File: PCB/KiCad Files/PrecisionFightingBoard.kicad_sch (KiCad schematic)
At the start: 6 parts, among them J1 Screw_Terminal_01x05, J2 Screw_Terminal_01x05, J3 Screw_Terminal_01x05, J4 Screw_Terminal_01x05, J5 Conn_02x10_Odd_Even, U1 Teensy4.0

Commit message: add mounting hole
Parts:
- added H1, H2, H3, H4: MountingHole, symbol Mechanical:MountingHole
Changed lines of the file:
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@@
     (pin "5")
     (instances
-      (project "Teensy"
+      (project "PrecisionFightingBoard"
         (path "/01d790aa-01e7-46c4-a23c-7deb91137dd0"
           (reference "J2") (unit 1)
+        )
+      )
+    )
+  )
+  (symbol (lib_id "Mechanical:MountingHole") (at 24.13 99.06 0) (unit 1)
+    (in_bom yes) (on_board yes) (dnp no) (fields_autoplaced)
+    (property "Reference" "H2" (at 26.67 97.79 0)
+      (effects (font (size 1.27 1.27)) (justify left))
+    )
+    (property "Value" "MountingHole" (at 26.67 100.33 0)
+      (effects (font (size 1.27 1.27)) (justify left))
+    )
+    (property "Footprint" "" (at 24.13 99.06 0)
+      (effects (font (size 1.27 1.27)) hide)
+    )
+    (property "Datasheet" "~" (at 24.13 99.06 0)
+      (effects (font (size 1.27 1.27)) hide)
+    )
+    (instances
+      (project "PrecisionFightingBoard"
+        (path "/01d790aa-01e7-46c4-a23c-7deb91137dd0"
+          (reference "H2") (unit 1)
+        )
+      )
+    )
+  )
+  (symbol (lib_id "Mechanical:MountingHole") (at 24.13 106.68 0) (unit 1)
+    (in_bom yes) (on_board yes) (dnp no) (fields_autoplaced)
+    (property "Reference" "H3" (at 26.67 105.41 0)
+      (effects (font (size 1.27 1.27)) (justify left))
+    )
+    (property "Value" "MountingHole" (at 26.67 107.95 0)
+      (effects (font (size 1.27 1.27)) (justify left))
+    )
+    (property "Footprint" "" (at 24.13 106.68 0)
+      (effects (font (size 1.27 1.27)) hide)
+    )
+    (property "Datasheet" "~" (at 24.13 106.68 0)
+      (effects (font (size 1.27 1.27)) hide)
+    )
+    (instances
+      (project "PrecisionFightingBoard"
+        (path "/01d790aa-01e7-46c4-a23c-7deb91137dd0"
+          (reference "H3") (unit 1)
         )
       )
@@
     (pin "4")
     (instances
-      (project "Teensy"
+      (project "PrecisionFightingBoard"
         (path "/01d790aa-01e7-46c4-a23c-7deb91137dd0"
           (reference "U1") (unit 1)
@@
     )
   )
+  (symbol (lib_id "Mechanical:MountingHole") (at 24.13 91.44 0) (unit 1)
+    (in_bom yes) (on_board yes) (dnp no) (fields_autoplaced)
+    (property "Reference" "H1" (at 26.67 90.17 0)
+      (effects (font (size 1.27 1.27)) (justify left))
+    )
+    (property "Value" "MountingHole" (at 26.67 92.71 0)
+      (effects (font (size 1.27 1.27)) (justify left))
+    )
+    (property "Footprint" "" (at 24.13 91.44 0)
+      (effects (font (size 1.27 1.27)) hide)
+    )
+    (property "Datasheet" "~" (at 24.13 91.44 0)
+      (effects (font (size 1.27 1.27)) hide)
+    )
+    (instances
+      (project "PrecisionFightingBoard"
+        (path "/01d790aa-01e7-46c4-a23c-7deb91137dd0"
+          (reference "H1") (unit 1)
+        )
+      )
+    )
+  )
+  (symbol (lib_id "Mechanical:MountingHole") (at 24.13 114.3 0) (unit 1)
+    (in_bom yes) (on_board yes) (dnp no) (fields_autoplaced)
+    (property "Reference" "H4" (at 26.67 113.03 0)
+      (effects (font (size 1.27 1.27)) (justify left))
+    )
+    (property "Value" "MountingHole" (at 26.67 115.57 0)
+      (effects (font (size 1.27 1.27)) (justify left))
+    )
+    (property "Footprint" "" (at 24.13 114.3 0)
+      (effects (font (size 1.27 1.27)) hide)
+    )
+    (property "Datasheet" "~" (at 24.13 114.3 0)
+      (effects (font (size 1.27 1.27)) hide)
+    )
+    (instances
+      (project "PrecisionFightingBoard"
+        (path "/01d790aa-01e7-46c4-a23c-7deb91137dd0"
+          (reference "H4") (unit 1)
+        )
+      )
+    )
+  )
   (symbol (lib_id "Connector:Screw_Terminal_01x05") (at 45.72 74.93 0) (unit 1)
     (in_bom yes) (on_board yes) (dnp no) (fields_autoplaced)
@@
     (pin "5")
     (instances
-      (project "Teensy"
+      (project "PrecisionFightingBoard"
         (path "/01d790aa-01e7-46c4-a23c-7deb91137dd0"
           (reference "J4") (unit 1)
@@
     (pin "5")
     (instances
-      (project "Teensy"
+      (project "PrecisionFightingBoard"
         (path "/01d790aa-01e7-46c4-a23c-7deb91137dd0"
           (reference "J3") (unit 1)
@@
     (pin "5")
     (instances
-      (project "Teensy"
+      (project "PrecisionFightingBoard"
         (path "/01d790aa-01e7-46c4-a23c-7deb91137dd0"
           (reference "J1") (unit 1)
@@
     (pin "9")
     (instances
-      (project "Teensy"
+      (project "PrecisionFightingBoard"
         (path "/01d790aa-01e7-46c4-a23c-7deb91137dd0"
           (reference "J5") (unit 1)

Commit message: Create a schematic
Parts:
- removed J1, J2, J3, J4: Screw_Terminal_01x05, symbol Connector:Screw_Terminal_01x05
- removed J5: Conn_02x10_Odd_Even, symbol Connector_Generic:Conn_02x10_Odd_Even
- added J10, J7, J8, J9: ST01x05, TerminalBlock_MetzConnect:TerminalBlock_MetzConnect_Type059_RT06305HBWC_1x05_P3.50mm_Horizontal, symbol Connector:Screw_Terminal_01x05
- added J6: Conn_02x10_Odd_Even, Connector_PinHeader_2.54mm:PinHeader_2x10_P2.54mm_Vertical, symbol Connector_Generic:Conn_02x10_Odd_Even
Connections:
- net GND: now reaches U1.1 (GND)
- net GND: now also J10.5 (Pin_5), J6.12 (Pin_12), J6.17 (Pin_17), J6.18 (Pin_18), J8.1 (Pin_1), J8.2 (Pin_2), J9.5 (Pin_5)
- net X: now reaches U1.10 (8_TX2_IN1)
- net X: now also J6.8 (Pin_8), J9.1 (Pin_1)
- net RB: now reaches U1.11 (9_OUT1C)
- net RB: now also J6.10 (Pin_10), J9.3 (Pin_3)
- net LB: now reaches U1.12 (10_CS_MQSR)
- net LB: now also J6.11 (Pin_11), J9.4 (Pin_4)
- net A: now reaches U1.13 (11_MOSI_CTX1)
- net A: now also J10.1 (Pin_1), J6.13 (Pin_13)
- net B: now reaches U1.14 (12_MISO_MQSL)
- net B: now also J10.2 (Pin_2), J6.14 (Pin_14)
- net UP: now reaches U1.2 (0_RX1_CRX2_CS1)
- net UP: now also J6.1 (Pin_1), J7.3 (Pin_3)
- net RT: now reaches U1.21 (14_A0_TX3_SPDIF_OUT)
- net RT: now also J10.3 (Pin_3), J6.15 (Pin_15)
- net LT: now reaches U1.22 (15_A1_RX3_SPDIF_IN)
- net LT: now also J10.4 (Pin_4), J6.16 (Pin_16)
- net L3: now reaches U1.25 (18_A4_SDA0)
- net R3: now reaches U1.26 (19_A5_SCL0)
- net DOWN: now reaches U1.3 (1_TX1_CTX2_MISO1)
- net DOWN: now also J6.2 (Pin_2), J7.2 (Pin_2)
- net LEFT: now reaches U1.4 (2_OUT2)
- net LEFT: now also J6.4 (Pin_4), J7.4 (Pin_4)
- net RIGHT: now reaches U1.5 (3_LRCLK2)
- net RIGHT: now also J6.3 (Pin_3), J7.5 (Pin_5)
- net HOME: now reaches U1.6 (4_BCLK2)
- net HOME: now also J6.6 (Pin_6), J8.3 (Pin_3)
- net BACK: now reaches U1.7 (5_IN2)
- net BACK: now also J6.5 (Pin_5), J8.4 (Pin_4)
- net START: now reaches U1.8 (6_OUT1D)
- net START: now also J6.7 (Pin_7), J8.5 (Pin_5)
- net Y: now reaches U1.9 (7_RX2_OUT1A)
- net Y: now also J6.9 (Pin_9), J9.2 (Pin_2)
- new net 5V: J6.19 (Pin_19), J6.20 (Pin_20), J7.1 (Pin_1)
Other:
- moved on the sheet: H1, H2, H3, H4, U1

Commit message: add GND wire
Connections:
- net GND: now also U1.32 (GND)
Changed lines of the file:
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@@
+    (stroke (width 0) (type default))
+  )
+  (wire (pts (xy 175.26 83.82) (xy 176.53 83.82))
     (stroke (width 0) (type default))
   )
@@
     (effects (font (size 1.27 1.27)) (justify left bottom))
   )
+  (label "GND" (at 176.53 83.82 0) (fields_autoplaced)
+    (effects (font (size 1.27 1.27)) (justify left bottom))
+  )

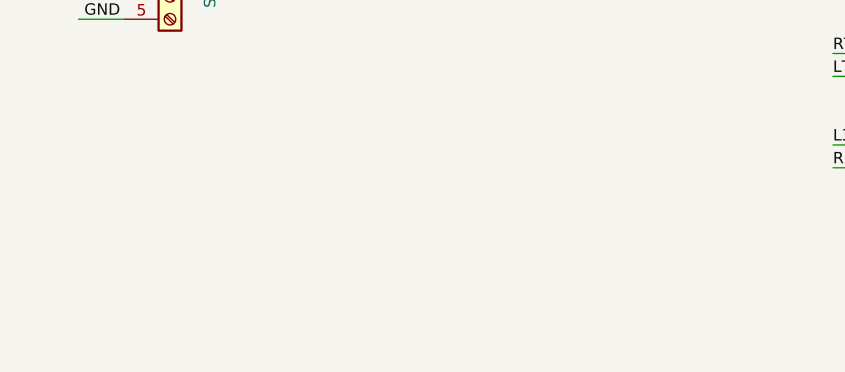
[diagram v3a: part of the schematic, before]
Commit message: add connector
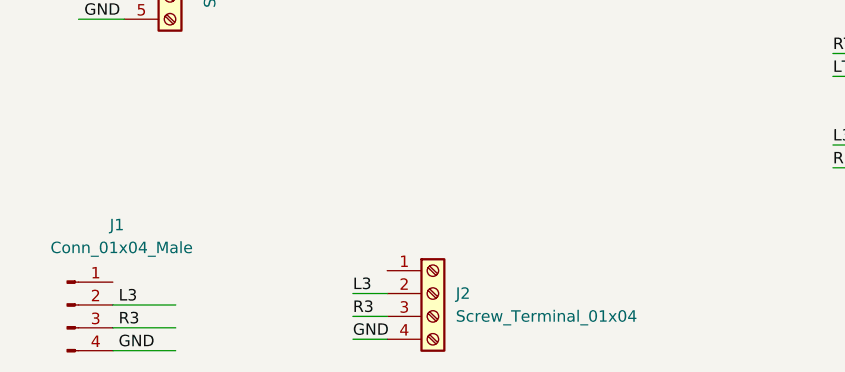
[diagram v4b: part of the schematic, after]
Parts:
- added J1: Conn_01x04_Male, Connector_JST:JST_PH_B4B-PH-K_1x04_P2.00mm_Vertical, symbol Connector:Conn_01x04_Male
- added J2: Screw_Terminal_01x04, symbol Connector:Screw_Terminal_01x04
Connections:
- net GND: now also J1.4 (Pin_4), J2.4 (Pin_4)
- net L3: now also J1.2 (Pin_2), J2.2 (Pin_2)
- net R3: now also J1.3 (Pin_3), J2.3 (Pin_3)
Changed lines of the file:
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@@
+    (stroke (width 0) (type default))
+  )
+  (wire (pts (xy 60.96 102.87) (xy 64.77 102.87))
     (stroke (width 0) (type default))
   )
@@
     (stroke (width 0) (type default))
   )
+  (wire (pts (xy 41.275 101.6) (xy 34.29 101.6))
+    (stroke (width 0) (type default))
+  )
   (wire (pts (xy 92.71 58.42) (xy 85.09 58.42))
     (stroke (width 0) (type default))
@@
     (stroke (width 0) (type default))
   )
+  (wire (pts (xy 41.275 104.14) (xy 34.29 104.14))
+    (stroke (width 0) (type default))
+  )
   (wire (pts (xy 35.56 46.99) (xy 30.48 46.99))
     (stroke (width 0) (type default))
@@
     (stroke (width 0) (type default))
   )
+  (wire (pts (xy 41.275 106.68) (xy 34.29 106.68))
+    (stroke (width 0) (type default))
+  )
   (wire (pts (xy 35.56 62.23) (xy 30.48 62.23))
     (stroke (width 0) (type default))
   )
+  (wire (pts (xy 60.96 100.33) (xy 64.77 100.33))
+    (stroke (width 0) (type default))
+  )
   (wire (pts (xy 35.56 69.85) (xy 30.48 69.85))
     (stroke (width 0) (type default))
@@
     (stroke (width 0) (type default))
   )
+  (wire (pts (xy 60.96 105.41) (xy 64.77 105.41))
+    (stroke (width 0) (type default))
+  )
   (label "START" (at 31.115 44.45 0) (fields_autoplaced)
     (effects (font (size 1.27 1.27)) (justify left bottom))
@@
     (effects (font (size 1.27 1.27)) (justify left bottom))
   )
+  (label "R3" (at 60.96 102.87 0) (fields_autoplaced)
+    (effects (font (size 1.27 1.27)) (justify left bottom))
+  )
   (label "BACK" (at 114.3 38.1 0) (fields_autoplaced)
     (effects (font (size 1.27 1.27)) (justify left bottom))
@@
     (effects (font (size 1.27 1.27)) (justify left bottom))
   )
+  (label "L3" (at 60.96 100.33 0) (fields_autoplaced)
+    (effects (font (size 1.27 1.27)) (justify left bottom))
+  )
   (label "GND" (at 31.115 69.85 0) (fields_autoplaced)
     (effects (font (size 1.27 1.27)) (justify left bottom))
@@
     (effects (font (size 1.27 1.27)) (justify left bottom))
   )
+  (label "L3" (at 34.925 101.6 0) (fields_autoplaced)
+    (effects (font (size 1.27 1.27)) (justify left bottom))
+  )
+  (label "GND" (at 60.96 105.41 0) (fields_autoplaced)
+    (effects (font (size 1.27 1.27)) (justify left bottom))
+  )
   (label "START" (at 114.3 40.64 0) (fields_autoplaced)
     (effects (font (size 1.27 1.27)) (justify left bottom))
@@
     (effects (font (size 1.27 1.27)) (justify left bottom))
   )
+  (label "GND" (at 34.925 106.68 0) (fields_autoplaced)
+    (effects (font (size 1.27 1.27)) (justify left bottom))
+  )
   (label "LT" (at 31.115 67.31 0) (fields_autoplaced)
+    (effects (font (size 1.27 1.27)) (justify left bottom))
+  )
+  (label "R3" (at 34.925 104.14 0) (fields_autoplaced)
     (effects (font (size 1.27 1.27)) (justify left bottom))
   )
@@
     )
   )
+  (symbol (lib_id "Connector:Conn_01x04_Male") (at 29.21 101.6 0) (unit 1)
+    (in_bom yes) (on_board yes) (dnp no)
+    (property "Reference" "J1" (at 35.56 92.71 0)
+      (effects (font (size 1.27 1.27)) (justify right))
+    )
+    (property "Value" "Conn_01x04_Male" (at 43.18 95.25 0)
+      (effects (font (size 1.27 1.27)) (justify right))
+    )
+    (property "Footprint" "Connector_JST:JST_PH_B4B-PH-K_1x04_P2.00mm_Vertical" (at 29.21 101.6 0)
+      (effects (font (size 1.27 1.27)) hide)
+    )
+    (property "Datasheet" "~" (at 29.21 101.6 0)
+      (effects (font (size 1.27 1.27)) hide)
+    )
+    (pin "1")
+    (pin "2")
+    (pin "3")
+    (pin "4")
+    (instances
+      (project "PrecisionFightingBoard"
+        (path "/01d790aa-01e7-46c4-a23c-7deb91137dd0"
+          (reference "J1") (unit 1)
+        )
+      )
+      (project "PicoFightingBoard"
+        (path "/e31110e5-ca51-423c-949c-39cc15aeefdb"
+          (reference "J4") (unit 1)
+        )
+      )
+    )
+  )
   (symbol (lib_id "Connector:Screw_Terminal_01x05") (at 40.64 39.37 0) (unit 1)
     (in_bom yes) (on_board yes) (dnp no)
@@
         )
       )
+    )
+  )
+  (symbol (lib_id "Connector:Screw_Terminal_01x04") (at 69.85 100.33 0) (unit 1)
+    (in_bom yes) (on_board yes) (dnp no) (fields_autoplaced)
+    (property "Reference" "J2" (at 72.39 100.33 0)
+      (effects (font (size 1.27 1.27)) (justify left))
+    )
+    (property "Value" "Screw_Terminal_01x04" (at 72.39 102.87 0)
+      (effects (font (size 1.27 1.27)) (justify left))
+    )
+    (property "Footprint" "" (at 69.85 100.33 0)
+      (effects (font (size 1.27 1.27)) hide)
+    )
+    (property "Datasheet" "~" (at 69.85 100.33 0)
+      (effects (font (size 1.27 1.27)) hide)
+    )
+    (pin "1")
+    (pin "2")
+    (pin "3")
+    (pin "4")
+    (instances
+      (project "PrecisionFightingBoard"
+        (path "/01d790aa-01e7-46c4-a23c-7deb91137dd0"
+          (reference "J2") (unit 1)
+        )
+      )

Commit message: create PCB
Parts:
- H1, H2, H3, H4: footprint (none) -> MountingHole:MountingHole_3.5mm
- J2: footprint (none) -> TerminalBlock_MetzConnect:TerminalBlock_MetzConnect_Type059_RT06304HBWC_1x04_P3.50mm_Horizontal
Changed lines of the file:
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@@
       (effects (font (size 1.27 1.27)) (justify left))
     )
-    (property "Footprint" "" (at 259.08 33.02 0)
+    (property "Footprint" "MountingHole:MountingHole_3.5mm" (at 259.08 33.02 0)
       (effects (font (size 1.27 1.27)) hide)
     )
@@
       (effects (font (size 1.27 1.27)) (justify left))
     )
-    (property "Footprint" "" (at 259.08 40.64 0)
+    (property "Footprint" "MountingHole:MountingHole_3.5mm" (at 259.08 40.64 0)
       (effects (font (size 1.27 1.27)) hide)
     )
@@
       (effects (font (size 1.27 1.27)) (justify left))
     )
-    (property "Footprint" "" (at 259.08 25.4 0)
+    (property "Footprint" "MountingHole:MountingHole_3.5mm" (at 259.08 25.4 0)
       (effects (font (size 1.27 1.27)) hide)
     )
@@
       (effects (font (size 1.27 1.27)) (justify left))
     )
-    (property "Footprint" "" (at 259.08 48.26 0)
+    (property "Footprint" "MountingHole:MountingHole_3.5mm" (at 259.08 48.26 0)
       (effects (font (size 1.27 1.27)) hide)
     )
@@
       (effects (font (size 1.27 1.27)) (justify left))
     )
-    (property "Footprint" "" (at 69.85 100.33 0)
-      (effects (font (size 1.27 1.27)) hide)
-    )
+    (property "Footprint" "TerminalBlock_MetzConnect:TerminalBlock_MetzConnect_Type059_RT06304HBWC_1x04_P3.50mm_Horizontal" (at 69.85 100.33 0)
+      (effects (font (size 1.27 1.27)) hide)
+    )
